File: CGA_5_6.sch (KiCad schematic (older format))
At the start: 4 parts, among them U13 74LS08, U15 74LS00, U20 74LS04, U21 74LS174

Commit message: More sheet 5
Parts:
- added U64: 74LS164, Package_DIP:DIP-14_W7.62mm_LongPads, symbol 74xx:74HC164
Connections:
- net GND: now also U64.7 (GND)
- net HSYNC_DLY: now also U64.9 (~MR)
- net VCC: now also U64.14 (VCC), U64.2 (DSB)
- new net LCLK: U64.8 (CP)
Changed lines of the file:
@@
 Text GLabel 4900 2000 2    50   Output ~ 0
 ~DISPEN_DLY
+$Comp
+L 74xx:74HC164 U64
+U 1 1 63FBDDCD
+P 2600 4050
+F 0 "U64" H 2350 4500 50  0000 C CNN
+F 1 "74LS164" H 2800 4500 50  0000 C CNN
+F 2 "Package_DIP:DIP-14_W7.62mm_LongPads" H 3500 3750 50  0001 C CNN
+F 3 "https://assets.nexperia.com/documents/data-sheet/74HC_HCT164.pdf" H 3500 3750 50  0001 C CNN
+	1    2600 4050
+	1    0    0    -1
+$EndComp
+$Comp
+L power:VCC #PWR?
+U 1 1 63FBFC7D
+P 2600 3550
+F 0 "#PWR?" H 2600 3400 50  0001 C CNN
+F 1 "VCC" H 2615 3723 50  0000 C CNN
+F 2 "" H 2600 3550 50  0001 C CNN
+F 3 "" H 2600 3550 50  0001 C CNN
+	1    2600 3550
+	1    0    0    -1
+$EndComp
+$Comp
+L power:GND #PWR?
+U 1 1 63FC038A
+P 2600 4650
+F 0 "#PWR?" H 2600 4400 50  0001 C CNN
+F 1 "GND" H 2605 4477 50  0000 C CNN
+F 2 "" H 2600 4650 50  0001 C CNN
+F 3 "" H 2600 4650 50  0001 C CNN
+	1    2600 4650
+	1    0    0    -1
+$EndComp
+$Comp
+L power:VCC #PWR?
+U 1 1 63FC5EE4
+P 1900 4250
+F 0 "#PWR?" H 1900 4100 50  0001 C CNN
+F 1 "VCC" H 1915 4423 50  0000 C CNN
+F 2 "" H 1900 4250 50  0001 C CNN
+F 3 "" H 1900 4250 50  0001 C CNN
+	1    1900 4250
+	1    0    0    -1
+$EndComp
+Wire Wire Line
+	2200 4150 2100 4150
+Wire Wire Line
+	2100 4150 2100 4300
+Wire Wire Line
+	2100 4300 1900 4300
+Wire Wire Line
+	1900 4300 1900 4250
+Text GLabel 1300 4350 0    50   Input ~ 0
+LCLK
+Wire Wire Line
+	2200 4350 1300 4350
+Text GLabel 1300 3850 0    50   Input ~ 0
+HSYNC_DLY
+Wire Wire Line
+	2200 3850 1300 3850
 $EndSCHEMATC

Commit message: More Sheet 5
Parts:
- added unit 2 of U15
- added U42: 74LS86, Package_DIP:DIP-14_W7.62mm_LongPads, symbol 74xx:74LS86
- added U43: 74S74, Package_DIP:DIP-14_W7.62mm_LongPads, symbol 74xx:74LS74
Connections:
- net HSYNC_DLY: now also U43.1 (~R)
- net LCLK: now also U43.3 (C)
- net at U64.1 (DSA): now also U42.8
- net at U64.13 (Q7): now also U15.4, U15.5, U43.2 (D)
- net at U64.6 (Q3): now also U42.10
- new net: U15.6, U42.9
- new net ~BW_2: U43.4 (~S)
- no-connect marks 0 -> 5
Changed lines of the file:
@@
 LCLK
 Wire Wire Line
-	2200 4350 1300 4350
+	2200 4350 1650 4350
 Text GLabel 1300 3850 0    50   Input ~ 0
 HSYNC_DLY
 Wire Wire Line
-	2200 3850 1300 3850
+	2200 3850 2000 3850
+$Comp
+L 74xx:74LS74 U43
+U 1 1 63FCF789
+P 5200 3250
+F 0 "U43" H 5050 3500 50  0000 C CNN
+F 1 "74S74" H 5400 3500 50  0000 C CNN
+F 2 "Package_DIP:DIP-14_W7.62mm_LongPads" H 5200 3250 50  0001 C CNN
+F 3 "74xx/74hc_hct74.pdf" H 5200 3250 50  0001 C CNN
+	1    5200 3250
+	1    0    0    -1
+$EndComp
+NoConn ~ 3000 4250
+NoConn ~ 3000 4150
+NoConn ~ 3000 3950
+NoConn ~ 3000 3750
+Wire Wire Line
+	2000 3850 2000 3250
+Wire Wire Line
+	2000 3250 4000 3250
+Wire Wire Line
+	4000 3250 4000 3650
+Wire Wire Line
+	4000 3650 5200 3650
+Wire Wire Line
+	5200 3650 5200 3550
+Connection ~ 2000 3850
+Wire Wire Line
+	2000 3850 1300 3850
+Wire Wire Line
+	3000 4450 4550 4450
+Wire Wire Line
+	4550 4450 4550 4050
+Wire Wire Line
+	4550 3150 4900 3150
+Wire Wire Line
+	1650 4350 1650 3150
+Wire Wire Line
+	1650 3150 4400 3150
+Wire Wire Line
+	4400 3150 4400 3250
+Wire Wire Line
+	4400 3250 4900 3250
+Connection ~ 1650 4350
+Wire Wire Line
+	1650 4350 1300 4350
+Text GLabel 4550 2850 0    50   Input ~ 0
+~BW_2
+Wire Wire Line
+	4550 2850 5200 2850
+Wire Wire Line
+	5200 2850 5200 2950
+NoConn ~ 5500 3350
+$Comp
+L 74xx:74LS00 U?
+U 2 1 63FF0248
+P 5250 4050
+AR Path="/60463C57/63FF0248" Ref="U?"  Part="4"
+AR Path="/60463CF3/63FF0248" Ref="U15"  Part="2"
+F 0 "U15" H 5250 4375 50  0000 C CNN
+F 1 "74LS00" H 5250 4284 50  0000 C CNN
+F 2 "Package_DIP:DIP-14_W7.62mm_LongPads" H 5250 4050 50  0001 C CNN
+F 3 "http://www.ti.com/lit/gpn/sn74ls00" H 5250 4050 50  0001 C CNN
+	2    5250 4050
+	1    0    0    -1
+$EndComp
+Wire Wire Line
+	4950 3950 4850 3950
+Wire Wire Line
+	4850 3950 4850 4050
+Wire Wire Line
+	4850 4150 4950 4150
+Wire Wire Line
+	4850 4050 4550 4050
+Connection ~ 4850 4050
+Wire Wire Line
+	4850 4050 4850 4150
+Connection ~ 4550 4050
+Wire Wire Line
+	4550 4050 4550 3150
+$Comp
+L 74xx:74LS86 U?
+U 3 1 640026CD
+P 6050 4150
+AR Path="/60463C10/640026CD" Ref="U?"  Part="4"
+AR Path="/60463C57/640026CD" Ref="U?"  Part="1"
+AR Path="/60463CF3/640026CD" Ref="U42"  Part="3"
+F 0 "U42" H 6050 4475 50  0000 C CNN
+F 1 "74LS86" H 6050 4384 50  0000 C CNN
+F 2 "Package_DIP:DIP-14_W7.62mm_LongPads" H 6050 4150 50  0001 C CNN
+F 3 "74xx/74ls86.pdf" H 6050 4150 50  0001 C CNN
+	3    6050 4150
+	1    0    0    -1
+$EndComp
+Wire Wire Line
+	5550 4050 5750 4050
+Wire Wire Line
+	3000 4050 3900 4050
+Wire Wire Line
+	3900 4050 3900 4550
+Wire Wire Line
+	3900 4550 5500 4550
+Wire Wire Line
+	5500 4550 5500 4250
+Wire Wire Line
+	5500 4250 5750 4250
+Wire Wire Line
+	6350 4150 6400 4150
+Wire Wire Line
+	6400 4150 6400 4950
+Wire Wire Line
+	6400 4950 1750 4950
+Wire Wire Line
+	1750 4950 1750 4050
+Wire Wire Line
+	1750 4050 2200 4050
 $EndSCHEMATC

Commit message: Sheet 5
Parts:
- added U14: 74LS32, Package_DIP:DIP-14_W7.62mm_LongPads, symbol 74xx:74LS32
- added unit 5 of U20
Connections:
- net at U64.12 (Q6): now also U20.11
- net at U43.5 (Q): now also U14.13
- new net: U14.12, U20.10
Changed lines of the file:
@@
 Wire Wire Line
 	1750 4050 2200 4050
+$Comp
+L 74xx:74LS32 U?
+U 4 1 6401699A
+P 7200 3250
+AR Path="/60463BAE/6401699A" Ref="U?"  Part="2"
+AR Path="/60463CF3/6401699A" Ref="U14"  Part="4"
+F 0 "U14" H 7200 2933 50  0000 C CNN
+F 1 "74LS32" H 7200 3024 50  0000 C CNN
+F 2 "Package_DIP:DIP-14_W7.62mm_LongPads" H 7200 3250 50  0001 C CNN
+F 3 "http://www.ti.com/lit/gpn/sn74LS32" H 7200 3250 50  0001 C CNN
+	4    7200 3250
+	1    0    0    1
+$EndComp
+Wire Wire Line
+	5500 3150 6900 3150
+$Comp
+L 74xx:74LS04 U?
+U 5 1 6402779D
+P 6450 3350
+AR Path="/60463C57/6402779D" Ref="U?"  Part="2"
+AR Path="/60463CC5/6402779D" Ref="U?"  Part="3"
+AR Path="/60463CF3/6402779D" Ref="U20"  Part="5"
+F 0 "U20" H 6400 3050 50  0000 C CNN
+F 1 "74LS04" H 6400 3150 50  0000 C CNN
+F 2 "Package_DIP:DIP-14_W7.62mm_LongPads" H 6450 3350 50  0001 C CNN
+F 3 "http://www.ti.com/lit/gpn/sn74LS04" H 6450 3350 50  0001 C CNN
+	5    6450 3350
+	1    0    0    -1
+$EndComp
+Wire Wire Line
+	6750 3350 6900 3350
+Wire Wire Line
+	6150 3350 6000 3350
+Wire Wire Line
+	6000 3350 6000 3750
+Wire Wire Line
+	6000 3750 6550 3750
+Wire Wire Line
+	6550 3750 6550 5050
+Wire Wire Line
+	6550 5050 3250 5050
+Wire Wire Line
+	3250 5050 3250 4350
+Wire Wire Line
+	3250 4350 3000 4350
 $EndSCHEMATC

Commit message: More sheet 5
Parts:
- added Q1: 2N3904, Package_TO_SOT_THT:TO-92_Inline, symbol Transistor_BJT:2N3904
- added R1: 75, Resistor_THT:R_Axial_DIN0207_L6.3mm_D2.5mm_P10.16mm_Horizontal, symbol Device:R_Small
- added R20: 360, Resistor_THT:R_Axial_DIN0207_L6.3mm_D2.5mm_P10.16mm_Horizontal, symbol Device:R_Small
- added R4: 20, Resistor_THT:R_Axial_DIN0207_L6.3mm_D2.5mm_P10.16mm_Horizontal, symbol Device:R_Small
- added R5, R7: 680, Resistor_THT:R_Axial_DIN0207_L6.3mm_D2.5mm_P10.16mm_Horizontal, symbol Device:R_Small
- added R6: 1k, Resistor_THT:R_Axial_DIN0207_L6.3mm_D2.5mm_P10.16mm_Horizontal, symbol Device:R_Small
- added R8: 750, Resistor_THT:R_Axial_DIN0207_L6.3mm_D2.5mm_P10.16mm_Horizontal, symbol Device:R_Small
- added unit 6 of U20
- added U24: 74LS244, Package_DIP:DIP-20_W7.62mm_LongPads, symbol 74xx:74LS244
- added U41: 74LS08, Package_DIP:DIP-14_W7.62mm_LongPads, symbol 74xx:74LS08
- added unit 2 of U42
- added U63: 74LS175, Package_DIP:DIP-16_W7.62mm_LongPads, symbol 74xx:74LS175
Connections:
- net GND: now also R1.1, U24.1 (OEa), U24.10 (GND), U63.8 (GND)
- net VCC: now also Q1.3 (C), R20.1, U24.20 (VCC), U63.16 (VCC), U63.4 (D0)
- net VSYNC_DLY: now also U63.1 (~Mr)
- net at U64.4 (Q1): now also U42.5, U63.9 (Cp)
- new net: U63.10 (Q2), U63.13 (D3)
- new net: U63.12 (D2), U63.7 (Q1)
- new net: U41.10, U63.14 (~Q3)
- new net: U41.9, U63.2 (Q0), U63.5 (D1)
- new net: U41.8, U42.4
- new net: U20.13, U42.6
- new net: U20.12, U24.2 (I0a)
- new net: R8.2, U24.12 (O3a)
- new net: R7.2, U24.14 (O2a)
- new net: R6.2, U24.16 (O1a)
- new net: R5.2, U24.18 (O0a)
- new net: Q1.2 (B), R20.2, R5.1, R6.1, R7.1, R8.1
- new net: Q1.1 (E), R1.2, R4.2
- new net COMP_VID: R4.1
- no-connect marks 5 -> 18

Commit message: More sheet 5
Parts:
- added C20, C21, C22, C23, C31, C32: 47p, Capacitor_THT:C_Disc_D4.3mm_W1.9mm_P5.00mm, symbol Device:C_Small
- added R17: 130, Resistor_THT:R_Axial_DIN0207_L6.3mm_D2.5mm_P10.16mm_Horizontal, symbol Device:R_Small
- added R18: 2k, Resistor_THT:R_Axial_DIN0207_L6.3mm_D2.5mm_P10.16mm_Horizontal, symbol Device:R_Small
- added R19: 3k, Resistor_THT:R_Axial_DIN0207_L6.3mm_D2.5mm_P10.16mm_Horizontal, symbol Device:R_Small
- added U62: 74LS125, Package_DIP:DIP-14_W10.16mm_LongPads, symbol 74xx:74LS125
- added U67: 74LS244, Package_DIP:DIP-20_W7.62mm_LongPads, symbol 74xx:74LS244
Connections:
- net GND: now also C20.2, C21.2, C22.2, C23.2, C31.2, C32.2, R17.2, U62.10, U62.13, U67.1 (OEa), U67.10 (GND), U67.19 (OEb)
- net VCC: now also U67.20 (VCC)
- net at U42.5, U63.9 (Cp), U64.4 (Q1): now also U67.11 (I0b)
- net at U41.8, U42.4: now also U67.13 (I1b)
- net G: now reaches U24.4 (I1a)
- net G: now also U67.4 (I1a)
- net I: now reaches U24.6 (I2a)
- net I: now also U67.8 (I3a)
- net at Q1.2 (B), R20.2, R5.1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: now also R17.1, R18.1, R19.1
- new net: U62.12, U62.8
- new net: R18.2, U67.3 (O3b)
- new net: R19.2, U67.5 (O2b)
- new net B: U67.15 (I2b), U67.6 (I2a)
- new net B_OUT: C22.1, U67.14 (O2a)
- new net G_OUT: C21.1, U67.16 (O1a)
- new net HSYNC_OUT: C32.1, U67.9 (O0b)
- new net I_OUT: C23.1, U67.12 (O3a)
- new net R: U67.17 (I3b), U67.2 (I0a)
- new net R_OUT: C20.1, U67.18 (O0a)
- new net SL: U62.11
- new net SL': U62.9
- new net VSYNC_OUT: C31.1, U67.7 (O1b)
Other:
- note added: "No value was specified in the original schematics.\nMy clone CGA card has 47pF caps at the RGBI output\nconnector."

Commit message: More sheet 5
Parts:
- added U45: 74LS151, Package_DIP:DIP-16_W7.62mm_LongPads, symbol 74xx:74LS151
- added U65: 74LS02, Package_DIP:DIP-14_W7.62mm_LongPads, symbol 74xx:74LS02
- added U68: 74LS86, Package_DIP:DIP-14_W7.62mm_LongPads, symbol 74xx:74LS86
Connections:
- net B: now also U45.11 (S0)
- net G: now also U68.1
- net GND: now also U45.4 (I0), U45.7 (~E), U45.8 (GND)
- net R: now also U68.4
- net VCC: now also U45.16 (VCC)
- net VSYNC_DLY: now also U65.9
- net at U14.11: now also U65.8
- new net: U65.10, U68.2, U68.5
- new net: U45.9 (S2), U68.6
- new net: U45.10 (S1), U68.3
- no-connect marks 18 -> 19
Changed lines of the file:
@@
 VSYNC_DLY
-Wire Wire Line
-	1250 6850 2100 6850
 Wire Wire Line
 	3100 5950 3150 5950
@@
 Wire Wire Line
 	4650 6050 5000 6050
+$Comp
+L 74xx:74LS02 U?
+U 3 1 64443C3F
+P 2150 9950
+AR Path="/60463C57/64443C3F" Ref="U?"  Part="4"
+AR Path="/60463CF3/64443C3F" Ref="U65"  Part="3"
+F 0 "U65" H 2150 10275 50  0000 C CNN
+F 1 "74LS02" H 2150 10184 50  0000 C CNN
+F 2 "Package_DIP:DIP-14_W7.62mm_LongPads" H 2150 9950 50  0001 C CNN
+F 3 "http://www.ti.com/lit/gpn/sn74ls02" H 2150 9950 50  0001 C CNN
+	3    2150 9950
+	1    0    0    1
+$EndComp
+Wire Wire Line
+	1250 6850 1500 6850
+Wire Wire Line
+	1850 9850 1500 9850
+Connection ~ 1500 6850
+Wire Wire Line
+	1500 6850 2100 6850
+Wire Wire Line
+	7500 3250 7650 3250
+Wire Wire Line
+	7650 3250 7650 4250
+Wire Wire Line
+	7650 4250 6650 4250
+Wire Wire Line
+	6650 4250 6650 5150
+Wire Wire Line
+	700  5150 6650 5150
+Wire Wire Line
+	700  10050 1850 10050
+$Comp
+L 74xx:74LS86 U?
+U 2 1 644BB5C8
+P 3200 10050
+AR Path="/60463C10/644BB5C8" Ref="U?"  Part="4"
+AR Path="/60463CF3/644BB5C8" Ref="U68"  Part="2"
+F 0 "U68" H 3200 10375 50  0000 C CNN
+F 1 "74LS86" H 3200 10284 50  0000 C CNN
+F 2 "Package_DIP:DIP-14_W7.62mm_LongPads" H 3200 10050 50  0001 C CNN
+F 3 "74xx/74ls86.pdf" H 3200 10050 50  0001 C CNN
+	2    3200 10050
+	1    0    0    1
+$EndComp
+Wire Wire Line
+	2450 9950 2700 9950
+Text GLabel 2600 10150 0    50   Input ~ 0
+R
+Wire Wire Line
+	2600 10150 2900 10150
+$Comp
+L 74xx:74LS86 U?
+U 1 1 6450EEF8
+P 3800 9550
+AR Path="/60463C10/6450EEF8" Ref="U?"  Part="4"
+AR Path="/60463CF3/6450EEF8" Ref="U68"  Part="1"
+F 0 "U68" H 3800 9875 50  0000 C CNN
+F 1 "74LS86" H 3800 9784 50  0000 C CNN
+F 2 "Package_DIP:DIP-14_W7.62mm_LongPads" H 3800 9550 50  0001 C CNN
+F 3 "74xx/74ls86.pdf" H 3800 9550 50  0001 C CNN
+	1    3800 9550
+	1    0    0    -1
+$EndComp
+Wire Wire Line
+	3500 9650 2700 9650
+Wire Wire Line
+	2700 9650 2700 9950
+Connection ~ 2700 9950
+Wire Wire Line
+	2700 9950 2900 9950
+Text GLabel 3200 9450 0    50   Input ~ 0
+G
+Wire Wire Line
+	3200 9450 3500 9450
+$Comp
+L 74xx:74LS151 U45
+U 1 1 6455FCDF
+P 5450 9050
+F 0 "U45" H 5200 9800 50  0000 C CNN
+F 1 "74LS151" H 5650 9800 50  0000 C CNN
+F 2 "Package_DIP:DIP-16_W7.62mm_LongPads" H 5450 9050 50  0001 C CNN
+F 3 "http://www.ti.com/lit/gpn/sn74LS151" H 5450 9050 50  0001 C CNN
+	1    5450 9050
+	1    0    0    -1
+$EndComp
+$Comp
+L power:GND #PWR?
+U 1 1 64564397
+P 5450 10050
+F 0 "#PWR?" H 5450 9800 50  0001 C CNN
+F 1 "GND" H 5455 9877 50  0000 C CNN
+F 2 "" H 5450 10050 50  0001 C CNN
+F 3 "" H 5450 10050 50  0001 C CNN
+	1    5450 10050
+	1    0    0    -1
+$EndComp
+$Comp
+L power:VCC #PWR?
+U 1 1 64565099
+P 5450 8150
+F 0 "#PWR?" H 5450 8000 50  0001 C CNN
+F 1 "VCC" H 5465 8323 50  0000 C CNN
+F 2 "" H 5450 8150 50  0001 C CNN
+F 3 "" H 5450 8150 50  0001 C CNN
+	1    5450 8150
+	1    0    0    -1
+$EndComp
+NoConn ~ 5950 8550
+Wire Wire Line
+	1500 6850 1500 9850
+Wire Wire Line
+	700  5150 700  10050
+Wire Wire Line
+	3500 10050 4550 10050
+Wire Wire Line
+	4550 10050 4550 9550
+Wire Wire Line
+	4550 9550 4950 9550
+Wire Wire Line
+	4450 9550 4450 9450
+Wire Wire Line
+	4450 9450 4950 9450
+Wire Wire Line
+	4100 9550 4450 9550
+Text GLabel 4300 9350 0    50   Input ~ 0
+B
+Wire Wire Line
+	4300 9350 4950 9350
+Wire Wire Line
+	4950 8450 4700 8450
+Wire Wire Line
+	4700 8450 4700 9750
+Wire Wire Line
+	4950 9750 4700 9750
+Connection ~ 4700 9750
+Wire Wire Line
+	4700 9750 4700 10050
+$Comp
+L power:GND #PWR?
+U 1 1 6461E739
+P 4700 10050
+F 0 "#PWR?" H 4700 9800 50  0001 C CNN
+F 1 "GND" H 4705 9877 50  0000 C CNN
+F 2 "" H 4700 10050 50  0001 C CNN
+F 3 "" H 4700 10050 50  0001 C CNN
+	1    4700 10050
+	1    0    0    -1
+$EndComp
 $EndSCHEMATC

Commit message: More sheet 5
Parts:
- added unit 2 of U43
- added U44: 74S74, Package_DIP:DIP-14_W7.62mm_LongPads, symbol 74xx:74LS74
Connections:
- net VCC: now also U45.12 (I7)
- net ~BW_2: now also U43.10 (~S), U43.13 (~R)
- net at U24.8 (I3a): now also U45.5 (Z)
- net CYAN: now reaches U45.1 (I3)
- net CYAN: now also U44.6 (~Q)
- net YELLOW_BURST: now reaches U45.13 (I6)
- net YELLOW_BURST: now also U43.9 (Q), U44.2 (D)
- net MAGENTA: now reaches U45.14 (I5)
- net MAGENTA: now also U44.9 (Q)
- net RED: now reaches U45.15 (I4)
- net RED: now also U44.12 (D), U44.5 (Q)
- net GREEN: now reaches U45.2 (I2)
- net GREEN: now also U44.8 (~Q)
- net BLUE: now reaches U45.3 (I1)
- net BLUE: now also U43.8 (~Q)
- new net 14_Mhz: U43.11 (C), U44.3 (C)
- new net 3.58_Mhz: U43.12 (D)
- new net ~14_Mhz: U44.11 (C)
- new net ~BW_1: U44.1 (~R), U44.10 (~S), U44.13 (~R), U44.4 (~S)
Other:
- moved on the sheet: U45, U65C, U68A, U68B

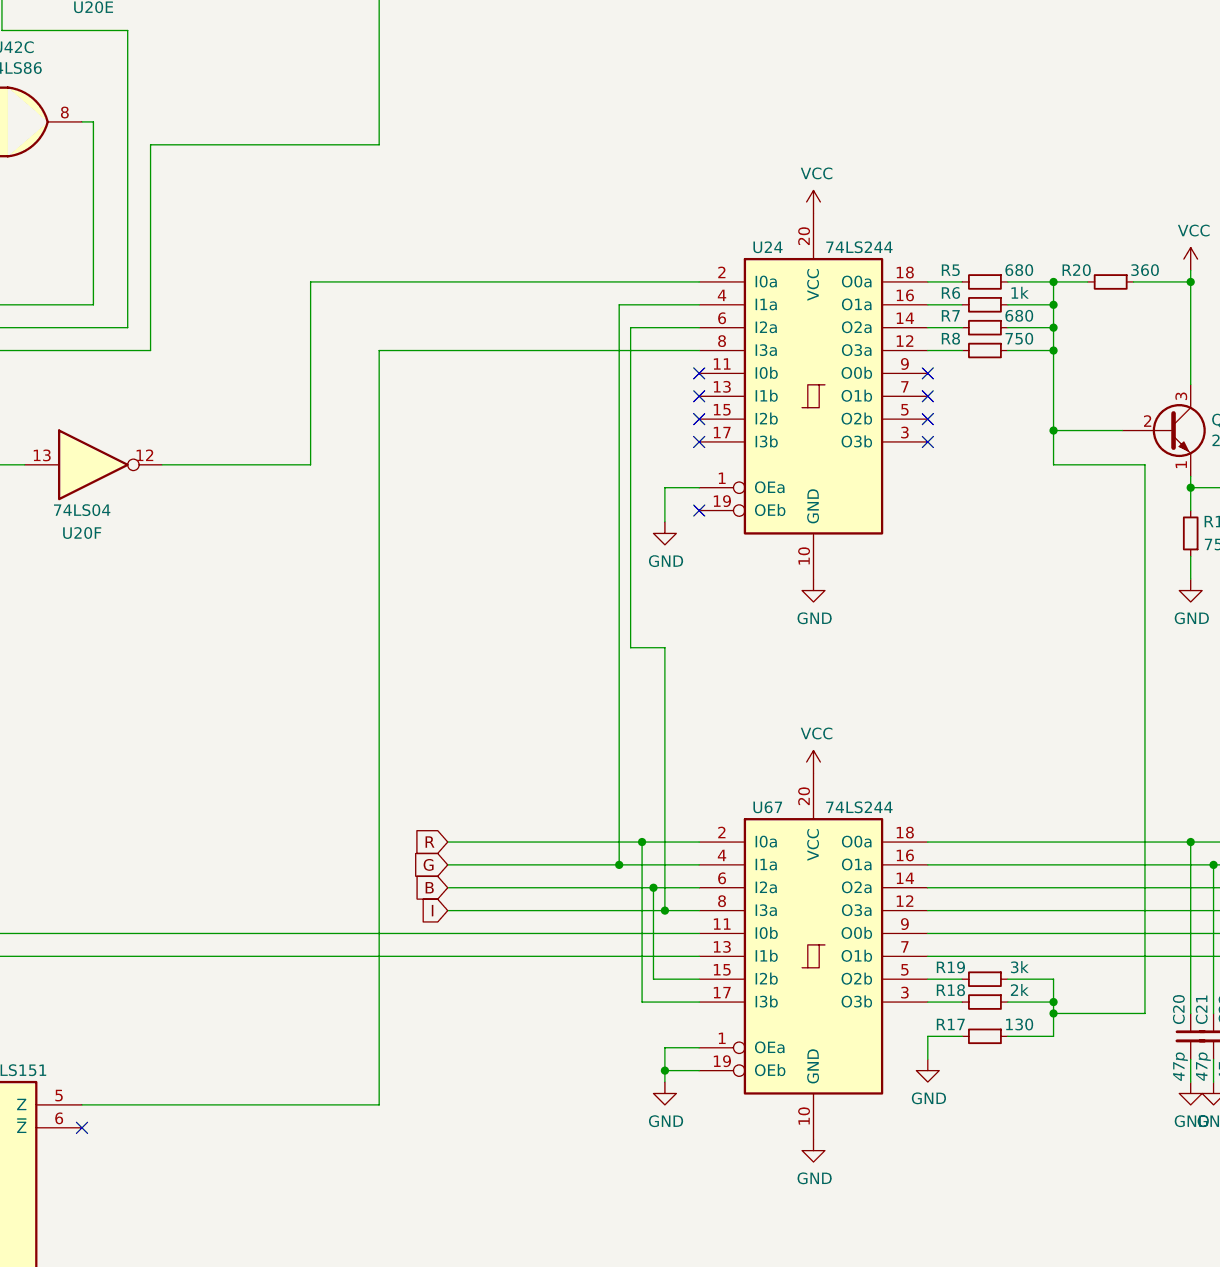
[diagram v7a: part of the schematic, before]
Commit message: Fixed some duplicate units and mislabeling
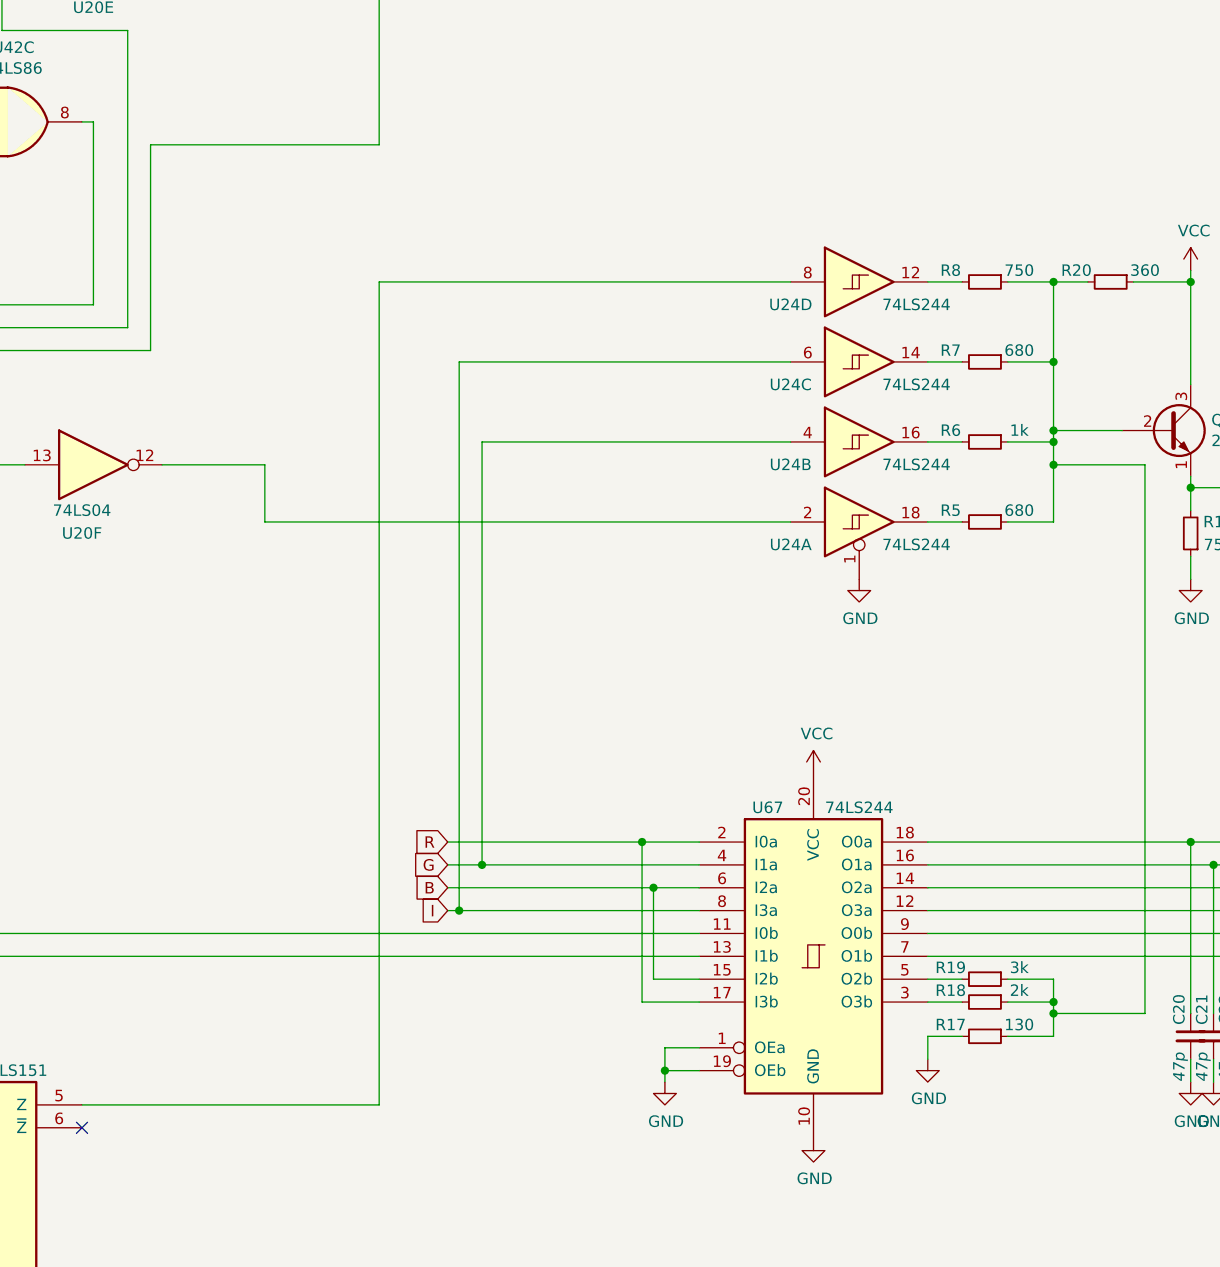
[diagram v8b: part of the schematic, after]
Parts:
- removed U24: 74LS244, Package_DIP:DIP-20_W7.62mm_LongPads, symbol 74xx:74LS244
- added U24: 74LS244, Package_DIP:DIP-20_W7.62mm_LongPads, symbol 74xx:74LS244_Split
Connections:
- net G: now also U24.4
- net GND: now also U24.1
- net I: now also U24.6
- net at U20.12: now also U24.2
- net at R8.2: now also U24.12
- net at R7.2: now also U24.14
- net at R6.2: now also U24.16
- net at R5.2: now also U24.18
- net at U45.5 (Z): now also U24.8
- no-connect marks 19 -> 10
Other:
- moved on the sheet: R5, R6, R7, R8
